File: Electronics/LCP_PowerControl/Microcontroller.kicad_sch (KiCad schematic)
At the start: 24 parts, among them J5 Conn_02x05_Odd_Even, Q1 DMG2305UX-7, SW1 SW_Push, U3 MSP430FR5989, Y1 32.768kHz

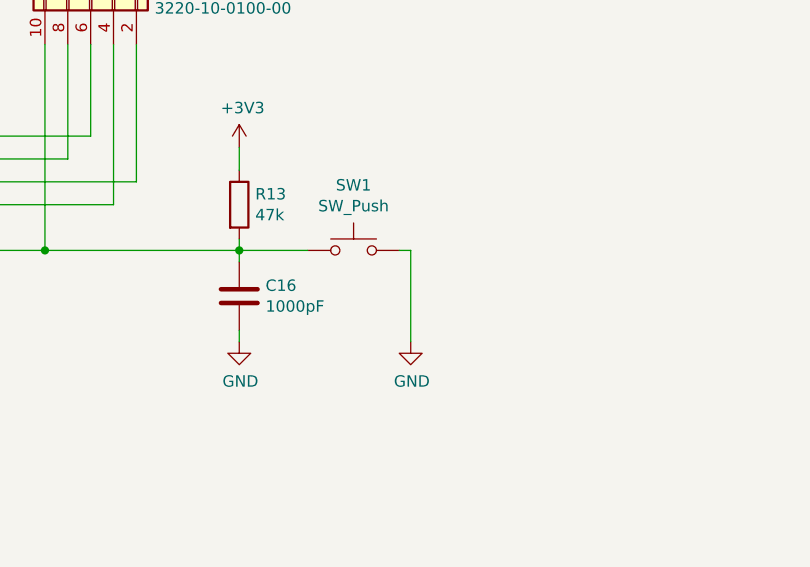
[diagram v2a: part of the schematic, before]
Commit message: fixed a silly loop
ESICI0 looped around the crystal keep-out region. Fixed that.
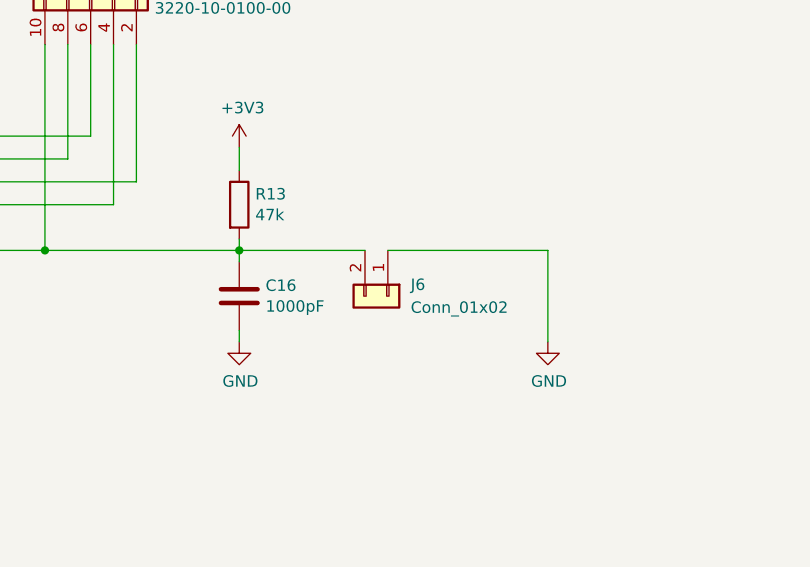
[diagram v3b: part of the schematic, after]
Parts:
- removed SW1: SW_Push, Button_Switch_SMD:SW_SPST_TL3305A, symbol Switch:SW_Push
- added J6: Conn_01x02, Connector_PinSocket_2.54mm:PinSocket_1x02_P2.54mm_Vertical, symbol Connector_Generic:Conn_01x02
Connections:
- net GND: now also J6.1 (Pin_1)
- net ~{RESET}: now also J6.2 (Pin_2)
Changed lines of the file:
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@@
-    (stroke (width 0) (type default))
-  )
-  (wire (pts (xy 308.61 88.9) (xy 316.23 88.9))
     (stroke (width 0) (type default))
   )
@@
     (stroke (width 0) (type default))
   )
-  (wire (pts (xy 327.66 88.9) (xy 326.39 88.9))
-    (stroke (width 0) (type default))
-  )
   (wire (pts (xy 267.97 171.45) (xy 273.05 171.45))
     (stroke (width 0) (type default))
@@
     (stroke (width 0) (type default))
   )
+  (wire (pts (xy 325.12 88.9) (xy 342.9 88.9))
+    (stroke (width 0) (type default))
+  )
   (wire (pts (xy 289.56 78.74) (xy 289.56 66.04))
     (stroke (width 0) (type default))
@@
     (stroke (width 0) (type default))
   )
-  (wire (pts (xy 327.66 99.06) (xy 327.66 88.9))
+  (wire (pts (xy 342.9 99.06) (xy 342.9 88.9))
     (stroke (width 0) (type default))
   )
@@
   )
   (wire (pts (xy 308.61 90.17) (xy 308.61 88.9))
+    (stroke (width 0) (type default))
+  )
+  (wire (pts (xy 308.61 88.9) (xy 322.58 88.9))
     (stroke (width 0) (type default))
   )
@@
     )
   )
-  (symbol (lib_id "Switch:SW_Push") (at 321.31 88.9 0) (unit 1)
-    (in_bom yes) (on_board yes) (dnp no)
-    (property "Reference" "SW1" (at 321.31 81.661 0)
-      (effects (font (size 1.27 1.27)))
-    )
-    (property "Value" "SW_Push" (at 321.31 83.9724 0)
-      (effects (font (size 1.27 1.27)))
-    )
-    (property "Footprint" "Button_Switch_SMD:SW_SPST_TL3305A" (at 321.31 83.82 0)
-      (effects (font (size 1.27 1.27)) hide)
-    )
-    (property "Datasheet" "~" (at 321.31 83.82 0)
-      (effects (font (size 1.27 1.27)) hide)
-    )
-    (property "MPN" "TL3315NF100Q" (at 321.31 88.9 0)
-      (effects (font (size 1.27 1.27)) hide)
-    )
-    (pin "2")
-    (pin "1")
-    (instances
-      (project "LCP_PowerControl"
-        (path "/41d9a78b-a4de-4258-a1a2-a19eb582c73a/00000000-0000-0000-0000-00005ee2a5a7"
-          (reference "SW1") (unit 1)
-        )
-      )
-    )
-  )
-  (symbol (lib_id "power:GND") (at 327.66 99.06 0) (unit 1)
-    (in_bom yes) (on_board yes) (dnp no)
-    (property "Reference" "#PWR029" (at 327.66 105.41 0)
-      (effects (font (size 1.27 1.27)) hide)
-    )
-    (property "Value" "GND" (at 327.787 103.4542 0)
-      (effects (font (size 1.27 1.27)))
-    )
-    (property "Footprint" "" (at 327.66 99.06 0)
-      (effects (font (size 1.27 1.27)) hide)
-    )
-    (property "Datasheet" "" (at 327.66 99.06 0)
+  (symbol (lib_id "power:GND") (at 342.9 99.06 0) (unit 1)
+    (in_bom yes) (on_board yes) (dnp no)
+    (property "Reference" "#PWR029" (at 342.9 105.41 0)
+      (effects (font (size 1.27 1.27)) hide)
+    )
+    (property "Value" "GND" (at 343.027 103.4542 0)
+      (effects (font (size 1.27 1.27)))
+    )
+    (property "Footprint" "" (at 342.9 99.06 0)
+      (effects (font (size 1.27 1.27)) hide)
+    )
+    (property "Datasheet" "" (at 342.9 99.06 0)
       (effects (font (size 1.27 1.27)) hide)
     )
@@
         )
       )
+    )
+  )
+  (symbol (lib_id "Connector_Generic:Conn_01x02") (at 325.12 93.98 270) (unit 1)
+    (in_bom yes) (on_board yes) (dnp no) (fields_autoplaced)
+    (property "Reference" "J6" (at 327.66 92.71 90)
+      (effects (font (size 1.27 1.27)) (justify left))
+    )
+    (property "Value" "Conn_01x02" (at 327.66 95.25 90)
+      (effects (font (size 1.27 1.27)) (justify left))
+    )
+    (property "Footprint" "Connector_PinSocket_2.54mm:PinSocket_1x02_P2.54mm_Vertical" (at 325.12 93.98 0)
+      (effects (font (size 1.27 1.27)) hide)
+    )
+    (property "Datasheet" "~" (at 325.12 93.98 0)
+      (effects (font (size 1.27 1.27)) hide)
+    )
+    (pin "1")
+    (pin "2")
+    (instances
+      (project "LCP_PowerControl"
+        (path "/41d9a78b-a4de-4258-a1a2-a19eb582c73a/00000000-0000-0000-0000-00005ee2a5a7"
+          (reference "J6") (unit 1)
+        )
+      )
